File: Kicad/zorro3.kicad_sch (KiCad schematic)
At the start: 13 parts, among them CN1 Zorro3, U1 SN74ABT16543DGGR, U2 SN74ABT16543DGGR, U3 SN74ABT16543DGGR, U4 SN74ABT16543DGGR, U5 74LVC07APW_118, U6 SN74ABT16245ADGGR

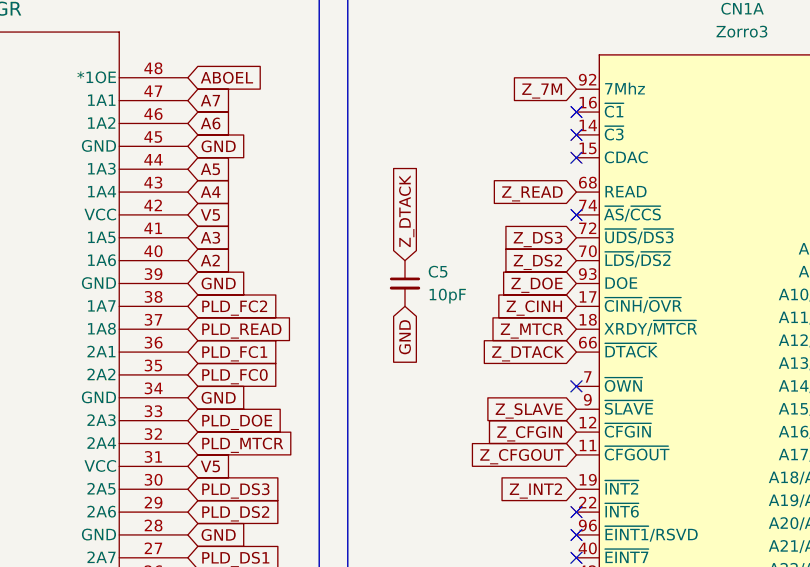
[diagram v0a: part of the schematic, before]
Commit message: Add more LCSC parts and mark some parts DNP
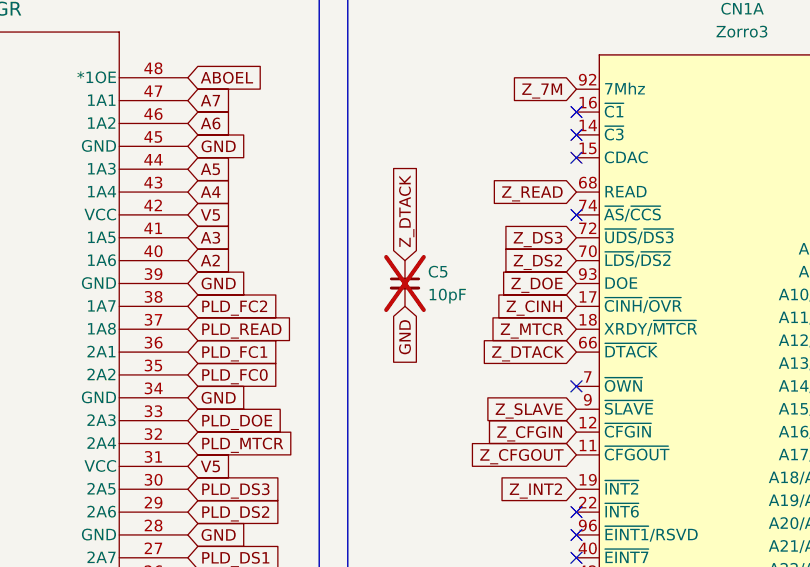
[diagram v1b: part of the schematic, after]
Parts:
- C5: now not fitted
- RN14, RN15, RN16: LCSC Part # (none) -> C784824
- U1, U2, U3, U4: LCSC Part # (none) -> C2865087
- U5: LCSC Part # (none) -> C6051
- U6: LCSC Part # (none) -> C130197
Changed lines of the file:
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@@
+			)
+		)
+		(property "LCSC Part #" "C784824"
+			(at 259.08 118.11 90)
+			(effects
+				(font
+					(size 1.27 1.27)
+				)
+				(hide yes)
 			)
 		)
@@
 			)
 		)
+		(property "LCSC Part #" "C784824"
+			(at 278.13 118.11 90)
+			(effects
+				(font
+					(size 1.27 1.27)
+				)
+				(hide yes)
+			)
+		)
 		(pin "1"
 		)
@@
 			)
 		)
+		(property "LCSC Part #" "C2865087"
+			(at 125.73 114.3 0)
+			(effects
+				(font
+					(size 1.27 1.27)
+				)
+				(hide yes)
+			)
+		)
 		(pin "8"
 		)
@@
 			)
 		)
+		(property "LCSC Part #" "C2865087"
+			(at 27.94 27.94 0)
+			(effects
+				(font
+					(size 1.27 1.27)
+				)
+				(hide yes)
+			)
+		)
 		(pin "53"
 		)
@@
 			)
 		)
+		(property "LCSC Part #" "C2865087"
+			(at 27.94 114.3 0)
+			(effects
+				(font
+					(size 1.27 1.27)
+				)
+				(hide yes)
+			)
+		)
 		(pin "44"
 		)
@@
 		)
 		(property "Description" ""
+			(at 43.18 219.71 0)
+			(effects
+				(font
+					(size 1.27 1.27)
+				)
+				(hide yes)
+			)
+		)
+		(property "LCSC Part #" "C6051"
 			(at 43.18 219.71 0)
 			(effects
@@
 		(in_bom yes)
 		(on_board yes)
-		(dnp no)
+		(dnp yes)
 		(fields_autoplaced yes)
 		(property "Reference" "C5"
@@
 			)
 		)
+		(property "LCSC Part #" "C784824"
+			(at 260.35 165.1 90)
+			(effects
+				(font
+					(size 1.27 1.27)
+				)
+				(hide yes)
+			)
+		)
 		(pin "1"
 		)
@@
 			)
 		)
+		(property "LCSC Part #" "C130197"
+			(at 237.49 26.67 0)
+			(effects
+				(font
+					(size 1.27 1.27)
+				)
+				(hide yes)
+			)
+		)
 		(pin "11"
 		)
@@
 			(at 125.73 26.67 0)
 			(effects
+				(font
+					(size 1.27 1.27)
+				)
+				(hide yes)
+			)
+		)
+		(property "LCSC Part #" "C2865087"
+			(at 125.73 26.67 0)
+			(effects

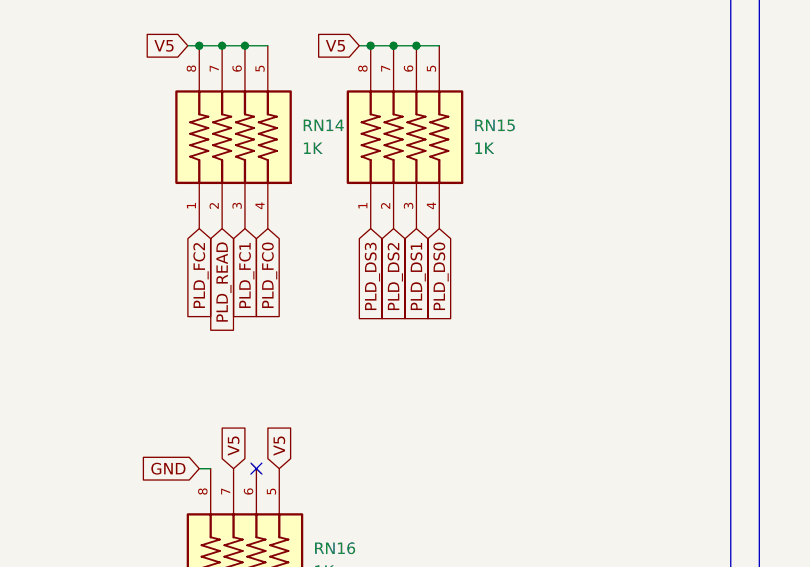
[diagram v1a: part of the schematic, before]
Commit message: RN15 pin swap
As requested in issue #7
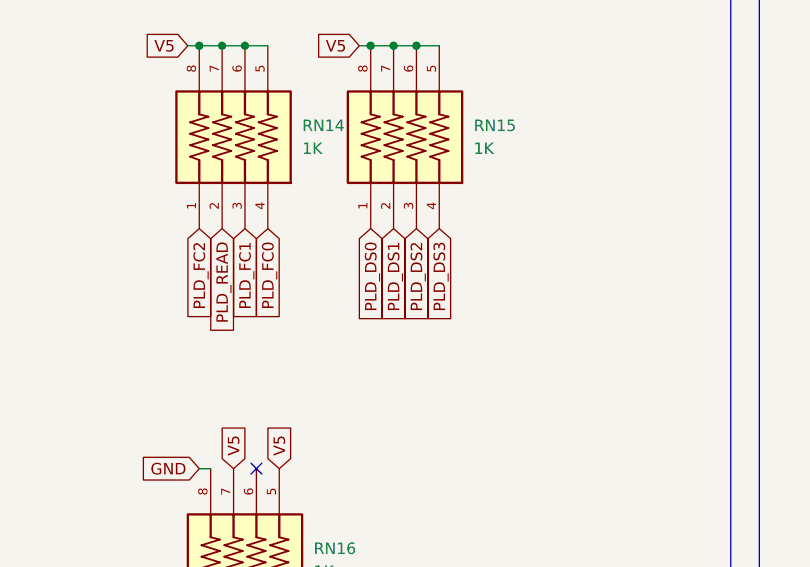
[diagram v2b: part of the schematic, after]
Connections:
- net PLD_DS0: now also RN15.1; no longer RN15.4
- net PLD_DS1: now also RN15.2; no longer RN15.3
- net PLD_DS2: now also RN15.3; no longer RN15.2
- net PLD_DS3: now also RN15.4; no longer RN15.1
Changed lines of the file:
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@@
 		)
 	)
-	(global_label "PLD_DS0"
-		(shape input)
-		(at 280.67 128.27 270)
-		(fields_autoplaced yes)
-		(effects
-			(font
-				(size 1.27 1.27)
-			)
-			(justify right)
-		)
-		(property "Intersheetrefs" "${INTERSHEET_REFS}"
-			(at 280.67 139.4799 90)
-			(effects
-				(font
-					(size 1.27 1.27)
-				)
-				(justify right)
-				(hide yes)
-			)
-		)
-	)
 	(global_label "Z_CFGIN"
 		(shape input)
@@
 		)
 	)
+	(global_label "PLD_DS1"
+		(shape input)
+		(at 275.59 128.27 270)
+		(fields_autoplaced yes)
+		(effects
+			(font
+				(size 1.27 1.27)
+			)
+			(justify right)
+		)
+		(property "Intersheetrefs" "${INTERSHEET_REFS}"
+			(at 275.59 139.4799 90)
+			(effects
+				(font
+					(size 1.27 1.27)
+				)
+				(justify right)
+				(hide yes)
+			)
+		)
+	)
 	(global_label "BMASTER"
 		(shape input)
@@
 		)
 	)
-	(global_label "PLD_DS3"
-		(shape input)
-		(at 273.05 128.27 270)
-		(fields_autoplaced yes)
-		(effects
-			(font
-				(size 1.27 1.27)
-			)
-			(justify right)
-		)
-		(property "Intersheetrefs" "${INTERSHEET_REFS}"
-			(at 273.05 139.4799 90)
-			(effects
-				(font
-					(size 1.27 1.27)
-				)
-				(justify right)
-				(hide yes)
-			)
-		)
-	)
 	(global_label "GND"
 		(shape input)
@@
 		)
 	)
+	(global_label "PLD_DS3"
+		(shape input)
+		(at 280.67 128.27 270)
+		(fields_autoplaced yes)
+		(effects
+			(font
+				(size 1.27 1.27)
+			)
+			(justify right)
+		)
+		(property "Intersheetrefs" "${INTERSHEET_REFS}"
+			(at 280.67 139.4799 90)
+			(effects
+				(font
+					(size 1.27 1.27)
+				)
+				(justify right)
+				(hide yes)
+			)
+		)
+	)
 	(global_label "Z_A12D4"
 		(shape input)
@@
 		)
 	)
+	(global_label "PLD_DS0"
+		(shape input)
+		(at 273.05 128.27 270)
+		(fields_autoplaced yes)
+		(effects
+			(font
+				(size 1.27 1.27)
+			)
+			(justify right)
+		)
+		(property "Intersheetrefs" "${INTERSHEET_REFS}"
+			(at 273.05 139.4799 90)
+			(effects
+				(font
+					(size 1.27 1.27)
+				)
+				(justify right)
+				(hide yes)
+			)
+		)
+	)
 	(global_label "Z_D17"
 		(shape input)
@@
 		)
 	)
+	(global_label "PLD_DS2"
+		(shape input)
+		(at 278.13 128.27 270)
+		(fields_autoplaced yes)
+		(effects
+			(font
+				(size 1.27 1.27)
+			)
+			(justify right)
+		)
+		(property "Intersheetrefs" "${INTERSHEET_REFS}"
+			(at 278.13 139.4799 90)
+			(effects
+				(font
+					(size 1.27 1.27)
+				)
+				(justify right)
+				(hide yes)
+			)
+		)
+	)
 	(global_label "D26"
 		(shape input)
@@
 		)
 	)
-	(global_label "PLD_DS2"
-		(shape input)
-		(at 275.59 128.27 270)
-		(fields_autoplaced yes)
-		(effects
-			(font
-				(size 1.27 1.27)
-			)
-			(justify right)
-		)
-		(property "Intersheetrefs" "${INTERSHEET_REFS}"
-			(at 275.59 139.4799 90)
-			(effects
-				(font
-					(size 1.27 1.27)
-				)
-				(justify right)
-				(hide yes)
-			)
-		)
-	)
 	(global_label "DBLT"
 		(shape input)
@@
 				(hide yes)
 			)
-		)
-	)
-	(global_label "PLD_DS1"
-		(shape input)
-		(at 278.13 128.27 270)
-		(fields_autoplaced yes)
-		(effects
-			(font
-				(size 1.27 1.27)
-			)
-			(justify right)
-		)
-		(property "Intersheetrefs" "${INTERSHEET_REFS}"
-			(at 278.13 139.4799 90)
-			(effects
-				(font
-					(size 1.27 1.27)
-				)
-				(justify right)
-				(hide yes)
-			)

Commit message: Pin swap on RN15 the right way
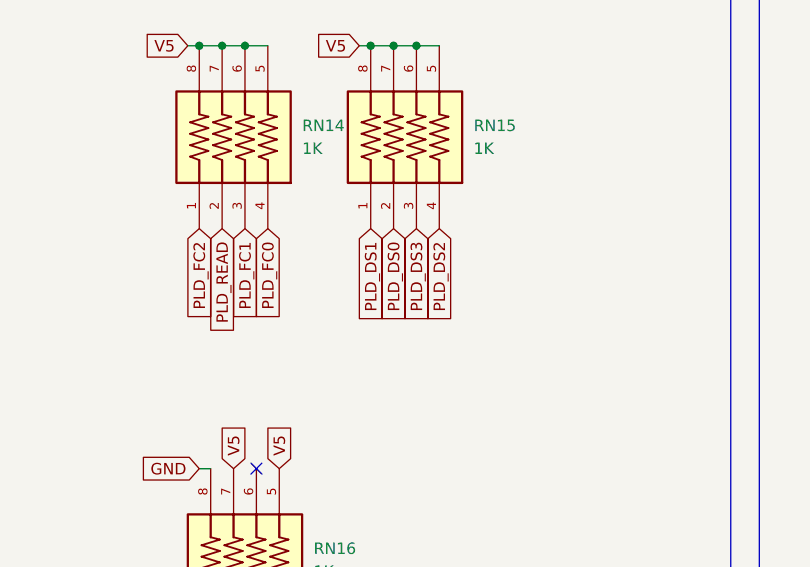
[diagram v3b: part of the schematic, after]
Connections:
- net PLD_DS0: now also RN15.2; no longer RN15.1
- net PLD_DS1: now also RN15.1; no longer RN15.2
- net PLD_DS2: now also RN15.4; no longer RN15.3
- net PLD_DS3: now also RN15.3; no longer RN15.4
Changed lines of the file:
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@@
 		)
 	)
-	(global_label "PLD_DS1"
-		(shape input)
-		(at 275.59 128.27 270)
-		(fields_autoplaced yes)
-		(effects
-			(font
-				(size 1.27 1.27)
-			)
-			(justify right)
-		)
-		(property "Intersheetrefs" "${INTERSHEET_REFS}"
-			(at 275.59 139.4799 90)
-			(effects
-				(font
-					(size 1.27 1.27)
-				)
-				(justify right)
-				(hide yes)
-			)
-		)
-	)
 	(global_label "BMASTER"
 		(shape input)
@@
 		)
 	)
-	(global_label "PLD_DS3"
-		(shape input)
-		(at 280.67 128.27 270)
-		(fields_autoplaced yes)
-		(effects
-			(font
-				(size 1.27 1.27)
-			)
-			(justify right)
-		)
-		(property "Intersheetrefs" "${INTERSHEET_REFS}"
-			(at 280.67 139.4799 90)
-			(effects
-				(font
-					(size 1.27 1.27)
-				)
-				(justify right)
-				(hide yes)
-			)
-		)
-	)
 	(global_label "Z_A12D4"
 		(shape input)
@@
 		)
 	)
+	(global_label "PLD_DS3"
+		(shape input)
+		(at 278.13 128.27 270)
+		(fields_autoplaced yes)
+		(effects
+			(font
+				(size 1.27 1.27)
+			)
+			(justify right)
+		)
+		(property "Intersheetrefs" "${INTERSHEET_REFS}"
+			(at 278.13 139.4799 90)
+			(effects
+				(font
+					(size 1.27 1.27)
+				)
+				(justify right)
+				(hide yes)
+			)
+		)
+	)
 	(global_label "Z_A12D4"
 		(shape input)
@@
 		)
 	)
+	(global_label "PLD_DS1"
+		(shape input)
+		(at 273.05 128.27 270)
+		(fields_autoplaced yes)
+		(effects
+			(font
+				(size 1.27 1.27)
+			)
+			(justify right)
+		)
+		(property "Intersheetrefs" "${INTERSHEET_REFS}"
+			(at 273.05 139.4799 90)
+			(effects
+				(font
+					(size 1.27 1.27)
+				)
+				(justify right)
+				(hide yes)
+			)
+		)
+	)
 	(global_label "GND"
 		(shape input)
@@
 		)
 	)
-	(global_label "PLD_DS0"
+	(global_label "Z_D17"
 		(shape input)
-		(at 273.05 128.27 270)
+		(at 378.46 90.17 0)
 		(fields_autoplaced yes)
 		(effects
@@
 				(size 1.27 1.27)
 			)
-			(justify right)
+			(justify left)
 		)
 		(property "Intersheetrefs" "${INTERSHEET_REFS}"
-			(at 273.05 139.4799 90)
+			(at 387.3113 90.17 0)
 			(effects
 				(font
 					(size 1.27 1.27)
 				)
-				(justify right)
+				(justify left)
 				(hide yes)
 			)
 		)
 	)
-	(global_label "Z_D17"
+	(global_label "Z_A23D15"
 		(shape input)
-		(at 378.46 90.17 0)
+		(at 99.06 86.36 0)
 		(fields_autoplaced yes)
 		(effects
@@
 		)
 		(property "Intersheetrefs" "${INTERSHEET_REFS}"
-			(at 387.3113 90.17 0)
+			(at 111.4189 86.36 0)
 			(effects
 				(font
@@
 		)
 	)
-	(global_label "Z_A23D15"
+	(global_label "PLD_DS0"
 		(shape input)
-		(at 99.06 86.36 0)
+		(at 275.59 128.27 270)
 		(fields_autoplaced yes)
 		(effects
@@
 				(size 1.27 1.27)
 			)
-			(justify left)
+			(justify right)
 		)
 		(property "Intersheetrefs" "${INTERSHEET_REFS}"
-			(at 111.4189 86.36 0)
+			(at 275.59 139.4799 90)
 			(effects
 				(font
 					(size 1.27 1.27)
 				)
-				(justify left)
+				(justify right)
 				(hide yes)
 			)
@@
 		)
 	)
-	(global_label "PLD_DS2"
+	(global_label "D26"
 		(shape input)
-		(at 278.13 128.27 270)
+		(at 125.73 67.31 180)
 		(fields_autoplaced yes)
 		(effects
@@
 		)
 		(property "Intersheetrefs" "${INTERSHEET_REFS}"
-			(at 278.13 139.4799 90)
+			(at 119.0558 67.31 0)
 			(effects
 				(font
@@
 		)
 	)
-	(global_label "D26"
+	(global_label "BERR"
 		(shape input)
-		(at 125.73 67.31 180)
+		(at 43.18 232.41 180)
 		(fields_autoplaced yes)
 		(effects
@@
 		)
 		(property "Intersheetrefs" "${INTERSHEET_REFS}"
-			(at 119.0558 67.31 0)
+			(at 35.2358 232.41 0)
 			(effects
 				(font
@@
 		)
 	)
-	(global_label "BERR"
+	(global_label "PLD_DS2"
 		(shape input)
-		(at 43.18 232.41 180)
+		(at 280.67 128.27 270)
 		(fields_autoplaced yes)
 		(effects
@@
 		)
 		(property "Intersheetrefs" "${INTERSHEET_REFS}"
-			(at 35.2358 232.41 0)
+			(at 280.67 139.4799 90)
 			(effects
 				(font

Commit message: Fix LCSC parts issues
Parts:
- FB4, FB5: LCSC Part # (none) -> C95177
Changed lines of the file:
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@@
+			)
+		)
+		(property "LCSC Part #" "C95177"
+			(at 229.87 72.39 90)
+			(effects
+				(font
+					(size 1.27 1.27)
+				)
+				(hide yes)
 			)
 		)
@@
 			)
 		)
+		(property "LCSC Part #" ""
+			(at 322.58 49.53 0)
+			(effects
+				(font
+					(size 1.27 1.27)
+				)
+				(hide yes)
+			)
+		)
 		(pin "1"
 		)
@@
 			(effects
 				(font
+					(size 1.27 1.27)
+				)
+				(hide yes)
+			)
+		)
+		(property "LCSC Part #" "C95177"
+			(at 231.14 74.93 90)
+			(effects
+				(font

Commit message: Add fiducials and clean up schematics
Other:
- moved on the sheet: FB4, FB5, U1, U2, U3, U4, U5, U6
